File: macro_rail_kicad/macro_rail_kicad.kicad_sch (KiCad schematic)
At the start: 15 parts, among them J1 Battery, J2 Motor, J3 128x128 OLED, J4 GIMBAL, SW1 POWER, SW2 SHUTTER, SW3 PREVIOUS, SW4 NEXT, SW5 RESET, U1 Pico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

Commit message: Organized schematic.
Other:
- note added: "Buttons"
- note added: "Gimbal"
- note added: "Microcontroller"
- note added: "Motor Driver"
- note added: "OLED"
- note added: "Power"
- moved on the sheet: A1, C1, C2, C3, J1, J2, J3, J4, SW1, SW2A, SW3A, SW4A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

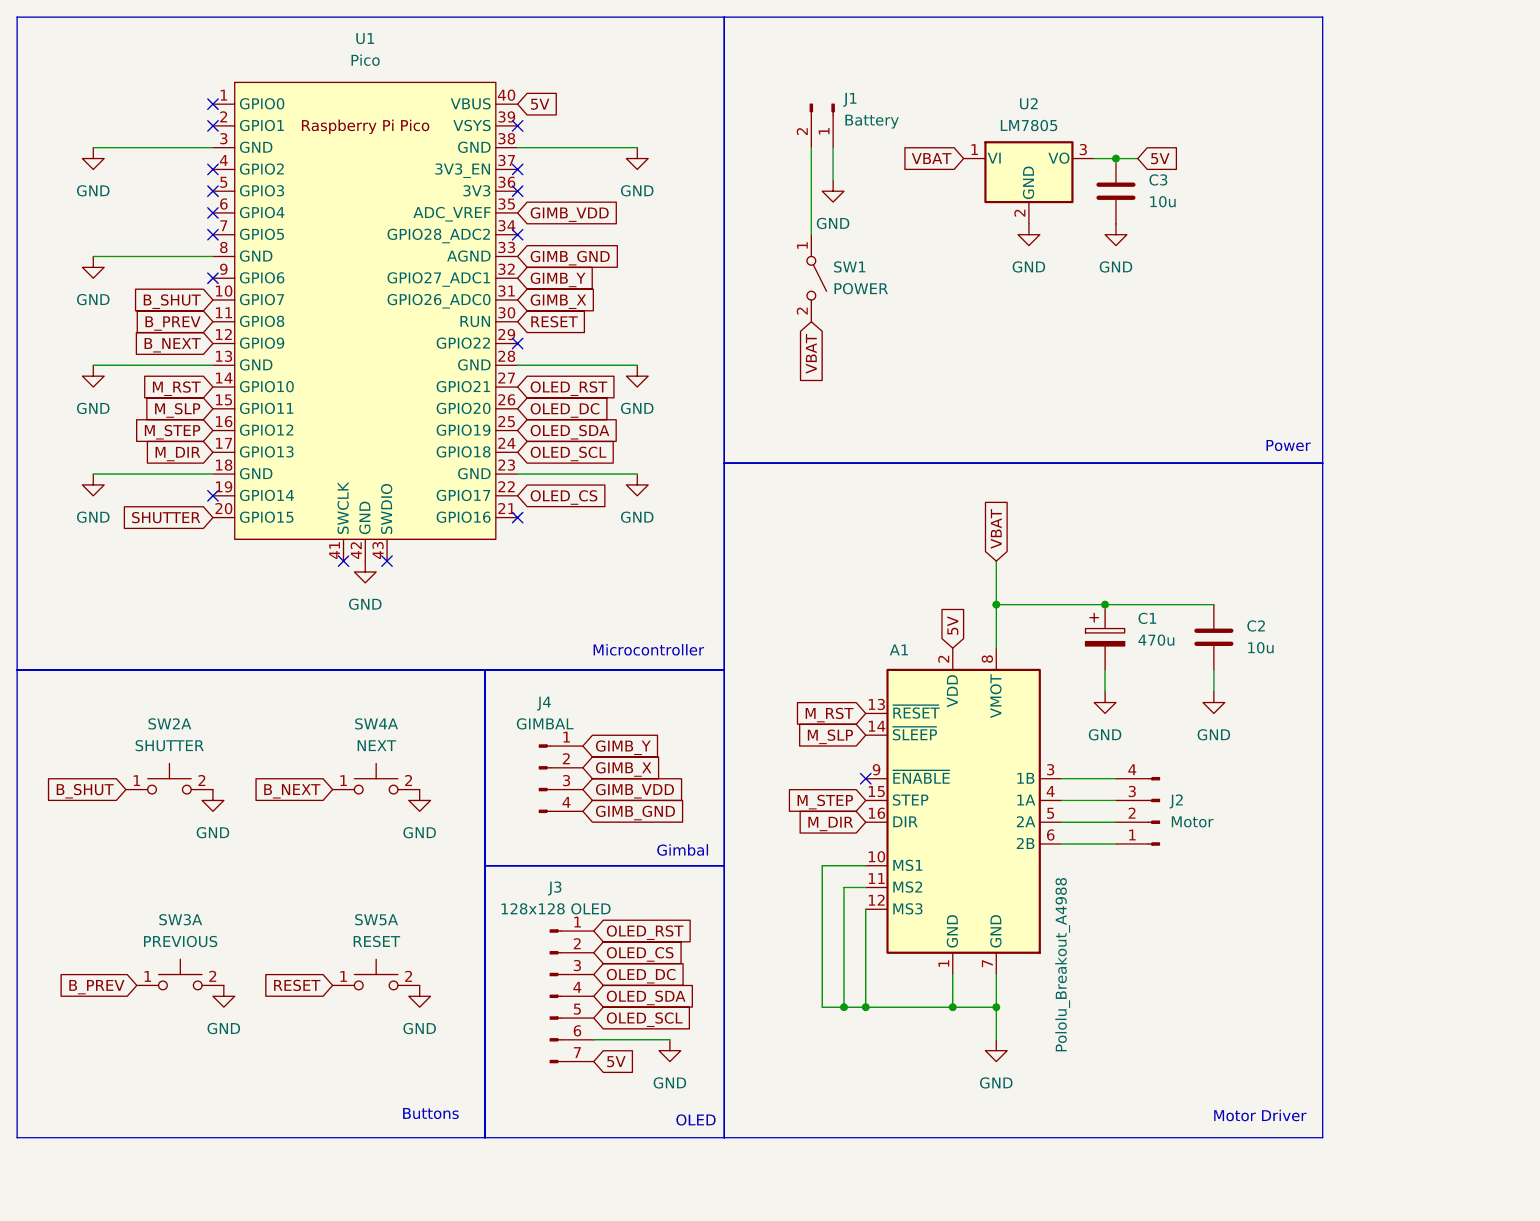
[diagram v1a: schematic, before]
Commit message: Added optocoupler and cleaned up ERC errors.
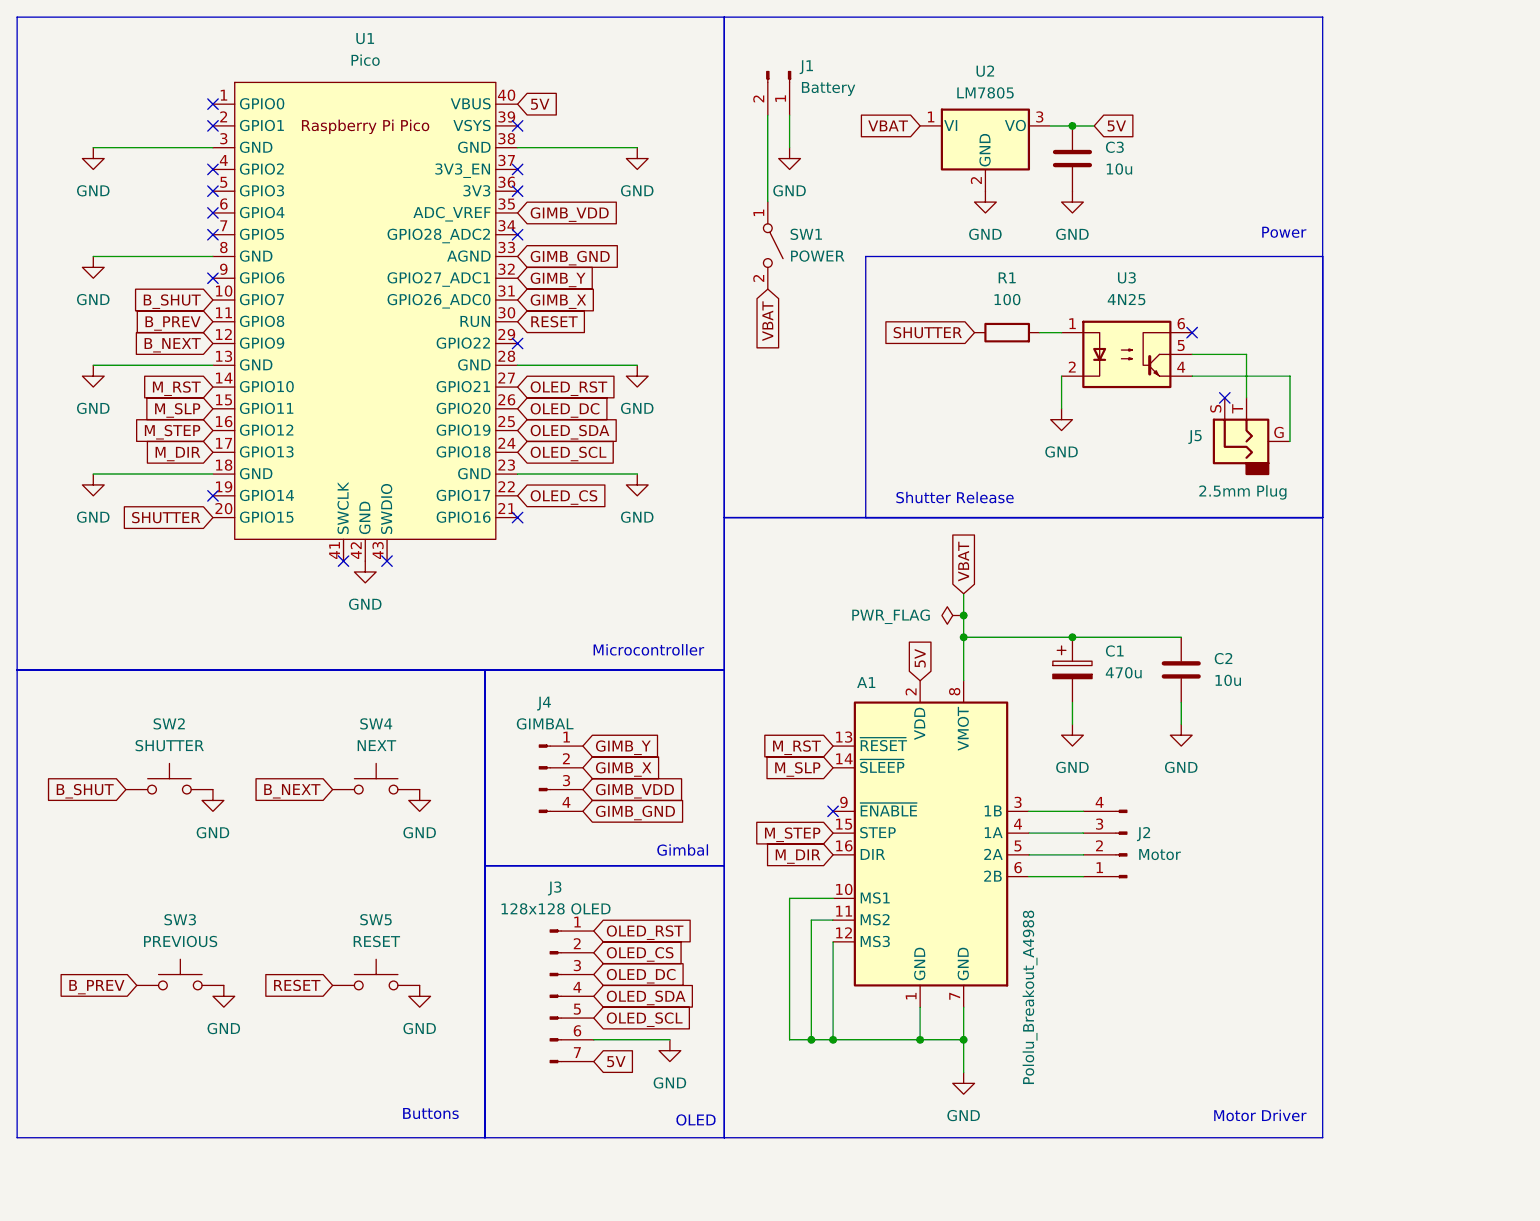
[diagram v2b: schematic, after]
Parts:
- added J5: 2.5mm Plug, Connector_PinHeader_2.54mm:PinHeader_1x02_P2.54mm_Horizontal, symbol Connector_Audio:AudioJack2_Ground
- added R1: 100, Resistor_THT:R_Axial_DIN0411_L9.9mm_D3.6mm_P12.70mm_Horizontal, symbol Device:R
- added U3: 4N25, Package_DIP:DIP-6_W7.62mm, symbol Isolator:4N25
- C1: footprint (none) -> Capacitor_THT:CP_Radial_D6.3mm_P2.50mm
- C2: footprint (none) -> Capacitor_THT:C_Disc_D3.8mm_W2.6mm_P2.50mm
- J1: footprint (none) -> Connector_PinHeader_2.54mm:PinHeader_1x02_P2.54mm_Vertical
- J2: footprint (none) -> Connector_PinHeader_2.54mm:PinHeader_1x04_P2.54mm_Vertical
- J3: footprint (none) -> Matt:OLED_128_128_1.5in
- SW2, SW3, SW4, SW5: symbol Switch:SW_Push_Dual_x2 -> Switch:SW_Push
- U1: footprint RP--Pico:RPi_Pico_SMD_TH -> RPi_Pico:RPi_Pico_SMD_TH
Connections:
- net GND: now also U3.2
- net SHUTTER: now also R1.1
- new net: R1.2, U3.1
- new net: J5.G, U3.4
- new net: J5.T, U3.5
- no-connect marks 17 -> 19
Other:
- note added: "Shutter Release"
- moved on the sheet: A1, C1, C2, C3, J1, J2, SW1, U2

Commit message: Fxied some footpring issues annd imported initial netlist into pcb.
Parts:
- C3: footprint (none) -> Capacitor_THT:C_Disc_D3.8mm_W2.6mm_P2.50mm
- U1: footprint RPi_Pico:RPi_Pico_SMD_TH -> RP-Pico:RPi_Pico_SMD_TH
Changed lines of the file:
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@@
 			)
 		)
-		(property "Footprint" "RPi_Pico:RPi_Pico_SMD_TH"
+		(property "Footprint" "RP-Pico:RPi_Pico_SMD_TH"
 			(at 78.74 50.8 90)
 			(effects
@@
 			)
 		)
-		(property "Footprint" ""
+		(property "Footprint" "Capacitor_THT:C_Disc_D3.8mm_W2.6mm_P2.50mm"
 			(at 162.2552 36.83 0)
 			(effects

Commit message: Finished draft of PCB
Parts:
- J4: footprint Connector_PinHeader_2.54mm:PinHeader_1x04_P2.54mm_Horizontal -> Connector_PinHeader_2.54mm:PinHeader_1x04_P2.54mm_Vertical
- J5: footprint Connector_PinHeader_2.54mm:PinHeader_1x02_P2.54mm_Horizontal -> Connector_PinHeader_2.54mm:PinHeader_1x02_P2.54mm_Vertical
- SW1: symbol Switch:SW_SPST -> Switch:SW_Push_DPDT
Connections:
- net B_NEXT: now also U1.10 (GPIO7); no longer U1.12 (GPIO9)
- net B_SHUT: now also U1.12 (GPIO9); no longer U1.10 (GPIO7)
- net GIMB_X: now also U1.32 (GPIO27_ADC1); no longer U1.31 (GPIO26_ADC0)
- net GIMB_Y: now also U1.31 (GPIO26_ADC0); no longer U1.32 (GPIO27_ADC1)
- net GND: no longer U1.42 (GND)
- net M_DIR: now also U1.14 (GPIO10); no longer U1.17 (GPIO13)
- net M_RST: now also U1.17 (GPIO13); no longer U1.14 (GPIO10)
- net M_SLP: now also U1.16 (GPIO12); no longer U1.15 (GPIO11)
- net M_STEP: now also U1.15 (GPIO11); no longer U1.16 (GPIO12)
- net VBAT: now also SW1.1 (A), SW1.4 (A); no longer SW1.2 (B)
- net at U3.4: now also J5.1; no longer J5.G
- net at U3.5: now also J5.2; no longer J5.T
- net at J1.2 (Pin_2): now also SW1.2 (B), SW1.5 (B); no longer SW1.1 (A)
- no-connect marks 19 -> 18
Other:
- moved on the sheet: J1
